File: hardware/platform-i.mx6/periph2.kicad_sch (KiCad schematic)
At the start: 12 parts, among them J4 USB_C_Receptacle_USB2.0, J9 PWM, U1 IMX6UL_BGA289

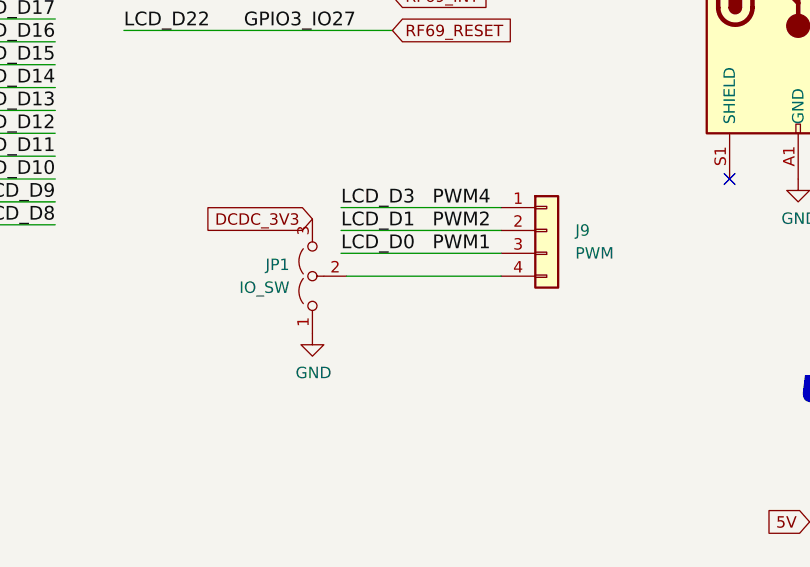
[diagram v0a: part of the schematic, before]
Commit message: Start reworking imx board into the new form factor
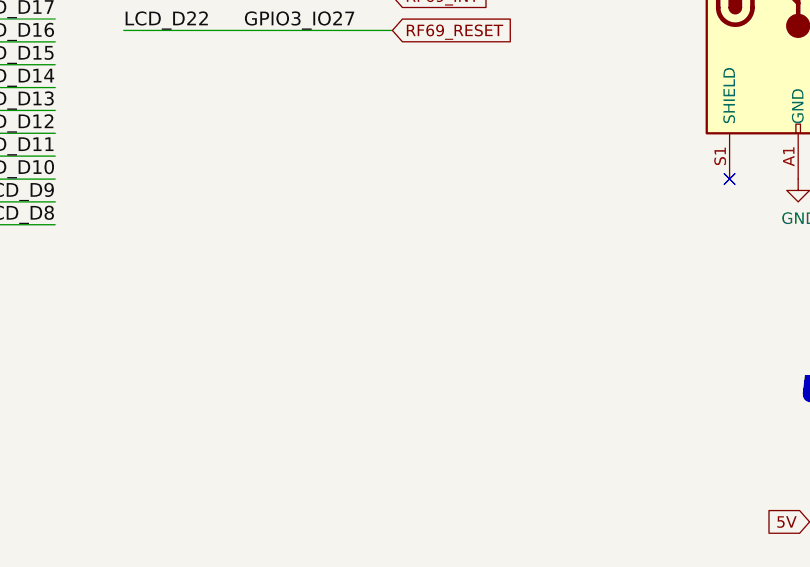
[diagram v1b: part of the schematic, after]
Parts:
- removed J9: PWM, Connector_JST:JST_SH_BM04B-SRSS-TB_1x04-1MP_P1.00mm_Vertical, symbol Connector_Generic:Conn_01x04
- removed JP1: IO_SW, Jumper:SolderJumper-3_P1.3mm_Open_RoundedPad1.0x1.5mm, symbol Jumper:Jumper_3_Open
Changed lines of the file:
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@@
-    (stroke (width 0) (type default) (color 0 0 0 0))
-  )
-  (wire (pts (xy 142.875 78.105) (xy 160.02 78.105))
     (stroke (width 0) (type default) (color 0 0 0 0))
   )
@@
     (stroke (width 0) (type default) (color 0 0 0 0))
   )
-  (wire (pts (xy 142.24 70.485) (xy 160.02 70.485))
-    (stroke (width 0) (type default) (color 0 0 0 0))
-  )
   (wire (pts (xy 31.75 34.29) (xy 54.61 34.29))
     (stroke (width 0) (type default) (color 0 0 0 0))
@@
     (stroke (width 0) (type default) (color 0 0 0 0))
   )
-  (wire (pts (xy 142.24 73.025) (xy 160.02 73.025))
-    (stroke (width 0) (type default) (color 0 0 0 0))
-  )
   (wire (pts (xy 210.82 49.53) (xy 210.82 46.99))
     (stroke (width 0) (type default) (color 0 0 0 0))
@@
   )
   (wire (pts (xy 209.55 29.21) (xy 224.79 29.21))
-    (stroke (width 0) (type default) (color 0 0 0 0))
-  )
-  (wire (pts (xy 142.24 75.565) (xy 160.02 75.565))
     (stroke (width 0) (type default) (color 0 0 0 0))
   )
@@
     (effects (font (size 1.524 1.524)) (justify right bottom))
   )
-  (label "PWM1" (at 152.4 75.565 0)
-    (effects (font (size 1.524 1.524)) (justify left bottom))
-  )
-  (label "LCD_D1" (at 142.24 73.025 0)
-    (effects (font (size 1.524 1.524)) (justify left bottom))
-  )
   (label "LCD_D22" (at 118.11 50.8 0)
     (effects (font (size 1.524 1.524)) (justify left bottom))
@@
   )
   (label "LCD_D6" (at 40.64 57.15 0)
-    (effects (font (size 1.524 1.524)) (justify left bottom))
-  )
-  (label "PWM4" (at 152.4 70.485 0)
     (effects (font (size 1.524 1.524)) (justify left bottom))
   )
@@
     (effects (font (size 1.27 1.27)) (justify left bottom))
   )
-  (label "PWM2" (at 152.4 73.025 0)
-    (effects (font (size 1.524 1.524)) (justify left bottom))
-  )
   (label "LCD_D13" (at 110.49 59.69 180)
     (effects (font (size 1.524 1.524)) (justify right bottom))
@@
     (effects (font (size 1.27 1.27)) (justify left bottom))
   )
-  (label "LCD_D0" (at 142.24 75.565 0)
-    (effects (font (size 1.524 1.524)) (justify left bottom))
-  )
   (label "GPIO3_IO27" (at 131.445 50.8 0)
     (effects (font (size 1.524 1.524)) (justify left bottom))
@@
   )
   (label "LCD_D3" (at 40.64 64.77 0)
-    (effects (font (size 1.524 1.524)) (justify left bottom))
-  )
-  (label "LCD_D3" (at 142.24 70.485 0)
     (effects (font (size 1.524 1.524)) (justify left bottom))
   )
@@
     (property "Intersheet References" "${INTERSHEET_REFS}" (id 0) (at 158.9273 46.9106 0)
       (effects (font (size 1.27 1.27)) (justify left) hide)
-    )
-  )
-  (global_label "DCDC_3V3" (shape input) (at 139.065 71.755 180) (fields_autoplaced)
-    (effects (font (size 1.27 1.27)) (justify right))
-    (property "Intersheet References" "${INTERSHEET_REFS}" (id 0) (at 111.125 37.465 0)
-      (effects (font (size 1.27 1.27)) hide)
     )
   )
@@
     (pin "1")
   )
-  (symbol (lib_id "Jumper:Jumper_3_Open") (at 139.065 78.105 90) (unit 1)
-    (in_bom yes) (on_board yes) (fields_autoplaced)
-    (property "Reference" "JP1" (id 0) (at 136.525 76.8349 90)
-      (effects (font (size 1.27 1.27)) (justify left))
-    )
-    (property "Value" "IO_SW" (id 1) (at 136.525 79.3749 90)
-      (effects (font (size 1.27 1.27)) (justify left))
-    )
-    (property "Footprint" "Jumper:SolderJumper-3_P1.3mm_Open_RoundedPad1.0x1.5mm" (id 2) (at 139.065 78.105 0)
-      (effects (font (size 1.27 1.27)) hide)
-    )
-    (property "Datasheet" "~" (id 3) (at 139.065 78.105 0)
-      (effects (font (size 1.27 1.27)) hide)
-    )
-    (property "DNP" "DNP" (id 4) (at 139.065 78.105 0)
-      (effects (font (size 1.27 1.27)) hide)
-    )
-    (pin "1")
-    (pin "2")
-    (pin "3")
-  )
-  (symbol (lib_id "power:GND") (at 139.065 84.455 0) (unit 1)
-    (in_bom yes) (on_board yes)
-    (property "Reference" "#PWR0125" (id 0) (at 139.065 90.805 0)
-      (effects (font (size 1.27 1.27)) hide)
-    )
-    (property "Value" "GND" (id 1) (at 139.192 88.8492 0))
-    (property "Footprint" "" (id 2) (at 139.065 84.455 0)
-      (effects (font (size 1.27 1.27)) hide)
-    )
-    (property "Datasheet" "" (id 3) (at 139.065 84.455 0)
-      (effects (font (size 1.27 1.27)) hide)
-    )
-    (pin "1")
-  )
   (symbol (lib_id "nano-rescue:R") (at 261.62 43.18 90) (unit 1)
     (in_bom yes) (on_board yes)
@@
     (pin "2")
   )
-  (symbol (lib_id "Connector_Generic:Conn_01x04") (at 165.1 73.025 0) (unit 1)
-    (in_bom yes) (on_board yes) (fields_autoplaced)
-    (property "Reference" "J9" (id 0) (at 168.275 73.0249 0)
-      (effects (font (size 1.27 1.27)) (justify left))
-    )
-    (property "Value" "PWM" (id 1) (at 168.275 75.5649 0)
-      (effects (font (size 1.27 1.27)) (justify left))
-    )
-    (property "Footprint" "Connector_JST:JST_SH_BM04B-SRSS-TB_1x04-1MP_P1.00mm_Vertical" (id 2) (at 165.1 73.025 0)
-      (effects (font (size 1.27 1.27)) hide)
-    )
-    (property "Datasheet" "~" (id 3) (at 165.1 73.025 0)
-      (effects (font (size 1.27 1.27)) hide)
-    )
-    (property "DNP" "DNP" (id 4) (at 165.1 73.025 0)
-      (effects (font (size 1.27 1.27)) hide)
-    )
-    (property "LCSC" "C265118" (id 5) (at 165.1 73.025 0)
-      (effects (font (size 1.27 1.27)) hide)
-    )
-    (property "MPN" "BM04B-PASS-TFT(LF)(SN)" (id 6) (at 165.1 73.025 0)
-      (effects (font (size 1.27 1.27)) hide)
-    )
-    (pin "1")
-    (pin "2")
-    (pin "3")
-    (pin "4")
-  )
   (symbol (lib_id "Connector:USB_C_Receptacle_USB2.0") (at 193.04 44.45 0) (unit 1)
